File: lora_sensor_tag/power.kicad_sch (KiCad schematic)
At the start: 36 parts, among them J2 Li-ion_bat_conn, Q3 NPN, U5 TPS63070RNMR, U6 MCP73871-2CAI_ML, U7 AMS1117-3.3, U8 MAX17048G_T10

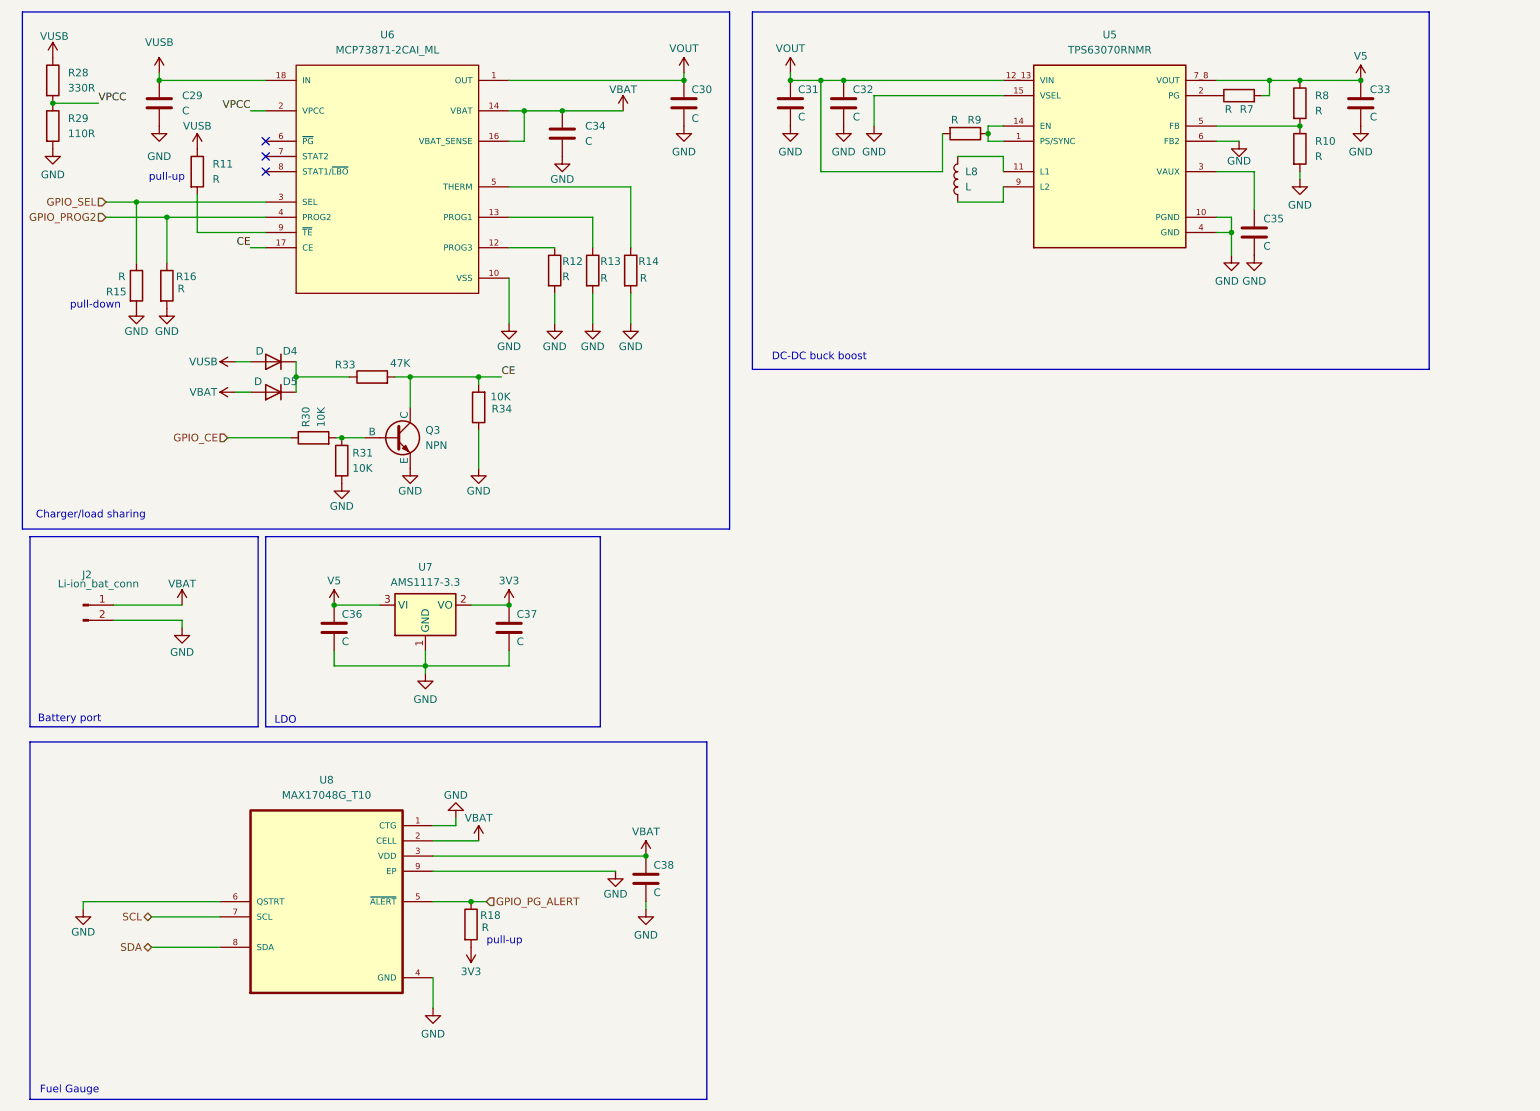
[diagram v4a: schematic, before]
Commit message: Large schematic update
This commit update the following:

 - Update MCP73871 CE control schematic
 - Finished schematic development and footprint
   assignment

Signed-off-by: Volodymyr <volodymyrnoha99@gmail.com>
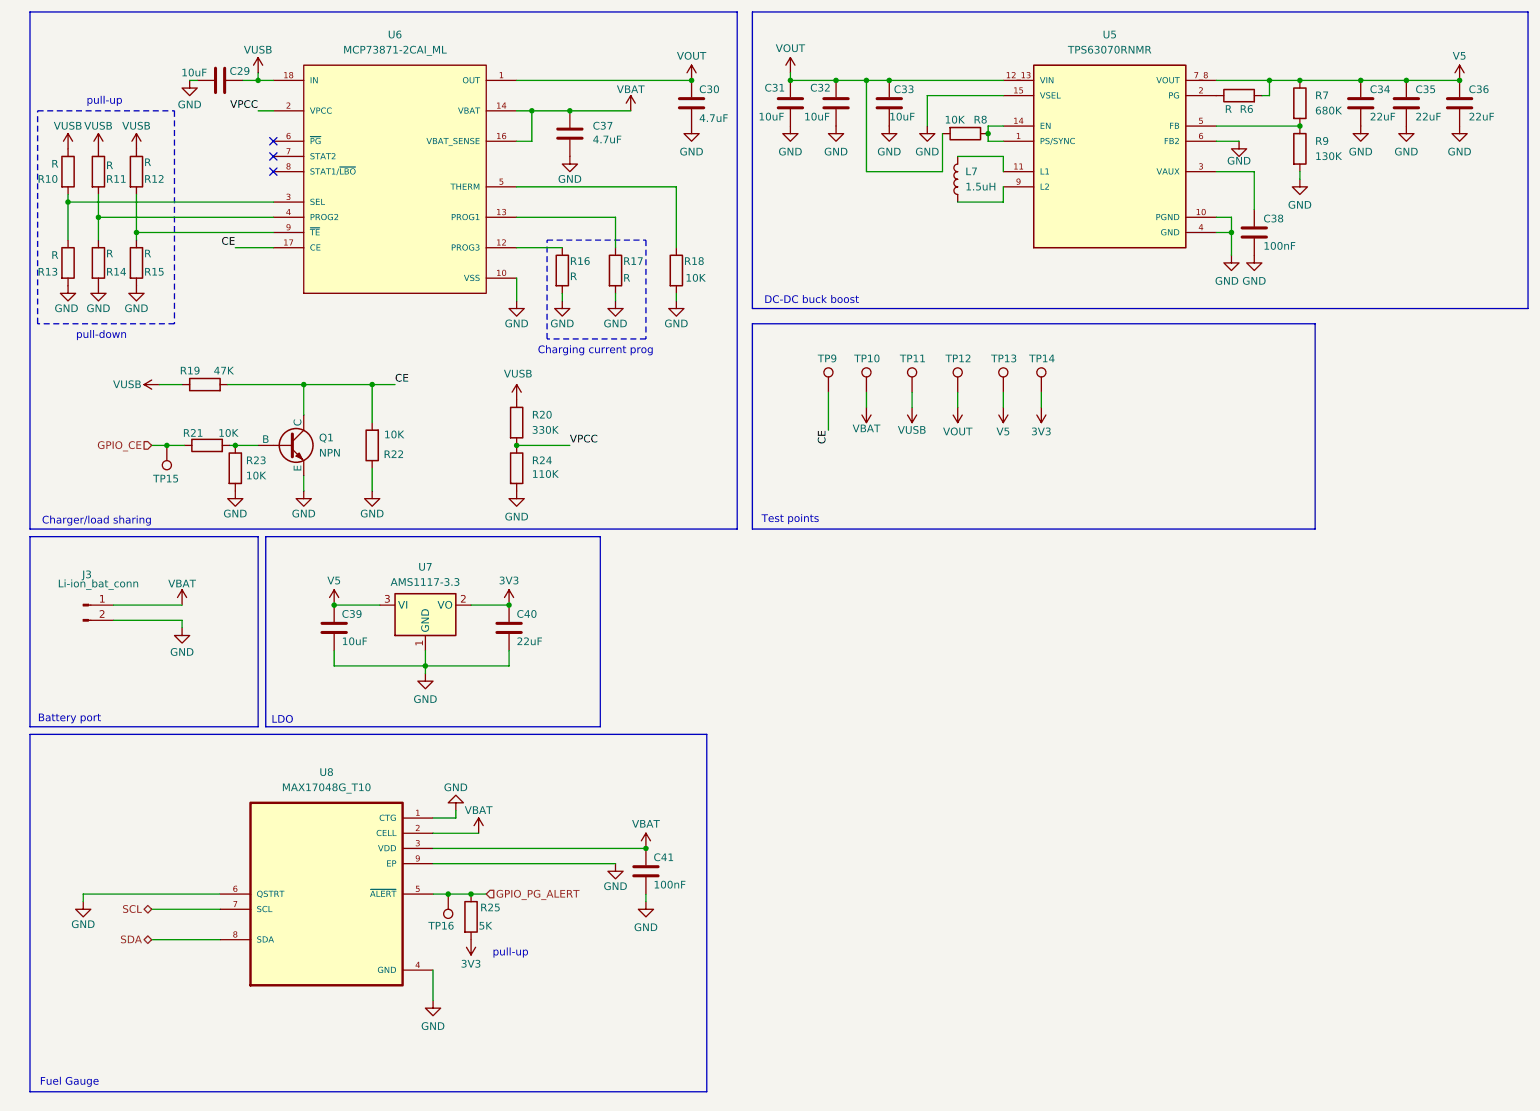
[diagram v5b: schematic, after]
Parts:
- removed D4, D5: D, symbol Device:D
- added C31: 10uF, Capacitor_SMD:C_0805_2012Metric, symbol Device:C
- added C35, C36: 22uF, Capacitor_SMD:C_0805_2012Metric, symbol Device:C
- added R10, R11, R15: R, Resistor_SMD:R_0603_1608Metric, symbol Device:R
- added TP10, TP11, TP12, TP13, TP14, TP15, TP16, TP9: TestPoint, TestPoint:TestPoint_Pad_D1.0mm, symbol Connector:TestPoint
- C29: value C -> 10uF; footprint (none) -> Capacitor_SMD:C_0603_1608Metric
- C30: value C -> 4.7uF; footprint MCP73871-2CAI_ML:QFN50P400X400X100-21N -> Capacitor_SMD:C_0603_1608Metric
- C32: renamed from C31; value C -> 10uF; footprint MCP73871-2CAI_ML:QFN50P400X400X100-21N -> Capacitor_SMD:C_0805_2012Metric
- C33: renamed from C32; value C -> 10uF; footprint MCP73871-2CAI_ML:QFN50P400X400X100-21N -> Capacitor_SMD:C_0603_1608Metric
- C34: renamed from C33; value C -> 22uF; footprint MCP73871-2CAI_ML:QFN50P400X400X100-21N -> Capacitor_SMD:C_0805_2012Metric
- C37: renamed from C34; value C -> 4.7uF; footprint (none) -> Capacitor_SMD:C_0603_1608Metric
- C38: renamed from C35; value C -> 100nF; footprint MCP73871-2CAI_ML:QFN50P400X400X100-21N -> Capacitor_SMD:C_0603_1608Metric
- C39: renamed from C36; value C -> 10uF; footprint MCP73871-2CAI_ML:QFN50P400X400X100-21N -> Capacitor_SMD:C_0603_1608Metric
- C40: renamed from C37; value C -> 22uF; footprint MCP73871-2CAI_ML:QFN50P400X400X100-21N -> Capacitor_SMD:C_0603_1608Metric
- C41: renamed from C38; value C -> 100nF; footprint MCP73871-2CAI_ML:QFN50P400X400X100-21N -> Capacitor_SMD:C_0603_1608Metric
- L7: renamed from L8; value L -> 1.5uH; footprint Relay_THT:Relay_DPDT_Finder_30.22 -> Inductor_SMD:L_Coilcraft_XxL4040
- Q1: renamed from Q3; footprint Package_DFN_QFN:Nordic_AQFN-94-1EP_7x7mm_P0.4mm -> Package_TO_SOT_SMD:SOT-23
- R12: renamed from R11; footprint TPS63070RNMR:VREG_TPS63070RNMR -> Resistor_SMD:R_0603_1608Metric
- R13: renamed from R15; footprint TPS63070RNMR:VREG_TPS63070RNMR -> Resistor_SMD:R_0603_1608Metric
- R14: renamed from R16; footprint TPS63070RNMR:VREG_TPS63070RNMR -> Resistor_SMD:R_0603_1608Metric
- R16: renamed from R12; footprint TPS63070RNMR:VREG_TPS63070RNMR -> Resistor_SMD:R_0603_1608Metric
- R17: renamed from R13; footprint TPS63070RNMR:VREG_TPS63070RNMR -> Resistor_SMD:R_0603_1608Metric
- R18: renamed from R14; value R -> 10K; footprint TPS63070RNMR:VREG_TPS63070RNMR -> Resistor_SMD:R_0603_1608Metric
- R19: renamed from R33; footprint TPS63070RNMR:VREG_TPS63070RNMR -> Resistor_SMD:R_0603_1608Metric
- R20: renamed from R28; value 330R -> 330K; footprint TPS63070RNMR:VREG_TPS63070RNMR -> Resistor_SMD:R_0603_1608Metric
- R21: renamed from R30; footprint TPS63070RNMR:VREG_TPS63070RNMR -> Resistor_SMD:R_0603_1608Metric
- R22: renamed from R34; footprint TPS63070RNMR:VREG_TPS63070RNMR -> Resistor_SMD:R_0603_1608Metric
- R23: renamed from R31; footprint TPS63070RNMR:VREG_TPS63070RNMR -> Resistor_SMD:R_0603_1608Metric
- R24: renamed from R29; value 110R -> 110K; footprint TPS63070RNMR:VREG_TPS63070RNMR -> Resistor_SMD:R_0603_1608Metric
- R25: renamed from R18; value R -> 5K; footprint TPS63070RNMR:VREG_TPS63070RNMR -> Resistor_SMD:R_0603_1608Metric
- R6: renamed from R7; footprint TPS63070RNMR:VREG_TPS63070RNMR -> Resistor_SMD:R_0603_1608Metric
- R7: renamed from R8; value R -> 680K; footprint TPS63070RNMR:VREG_TPS63070RNMR -> Resistor_SMD:R_0603_1608Metric
- R8: renamed from R9; value R -> 10K; footprint TPS63070RNMR:VREG_TPS63070RNMR -> Resistor_SMD:R_0603_1608Metric
- R9: renamed from R10; value R -> 130K; footprint TPS63070RNMR:VREG_TPS63070RNMR -> Resistor_SMD:R_0603_1608Metric
- renumbered J2 to J3
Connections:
- net 3V3: now also TP14.1
- net CE: now also TP9.1
- net GND: now also C29.1, C31.2, C35.2, C36.2, R15.2; no longer C29.2
- net GPIO_CE: now also TP15.1
- net GPIO_PG_ALERT: now also TP16.1
- net V5: now also C35.1, C36.1, TP13.1
- net VBAT: now also TP10.1
- net VOUT: now also C31.1, TP12.1
- net VUSB: now also C29.2, R19.1, R10.1, R11.1, TP11.1; no longer C29.1
- net at R12.2, U6.9 (~{TE}): now also R15.1
- net GPIO_PROG2: no longer names the net of R14.1, U6.4 (PROG2)
- net GPIO_PROG2: now also R11.2
- net GPIO_SEL: no longer names the net of R13.1, U6.3 (SEL)
- net GPIO_SEL: now also R10.2
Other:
- note added: "Charging current prog"
- note added: "Test points"
- moved on the sheet: C29, C30, C32, C33, C37, C41, Q1, R12, R13, R14, R16, R17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

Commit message: Update schematics
Adds the following updates to the schematics:
- Add power switch to the device;
- Add various LED indicators for device status monitoring;
- Add Reset and Prog buttons for device control;

Signed-off-by: Volodymyr <volodymyrnoha99@gmail.com>
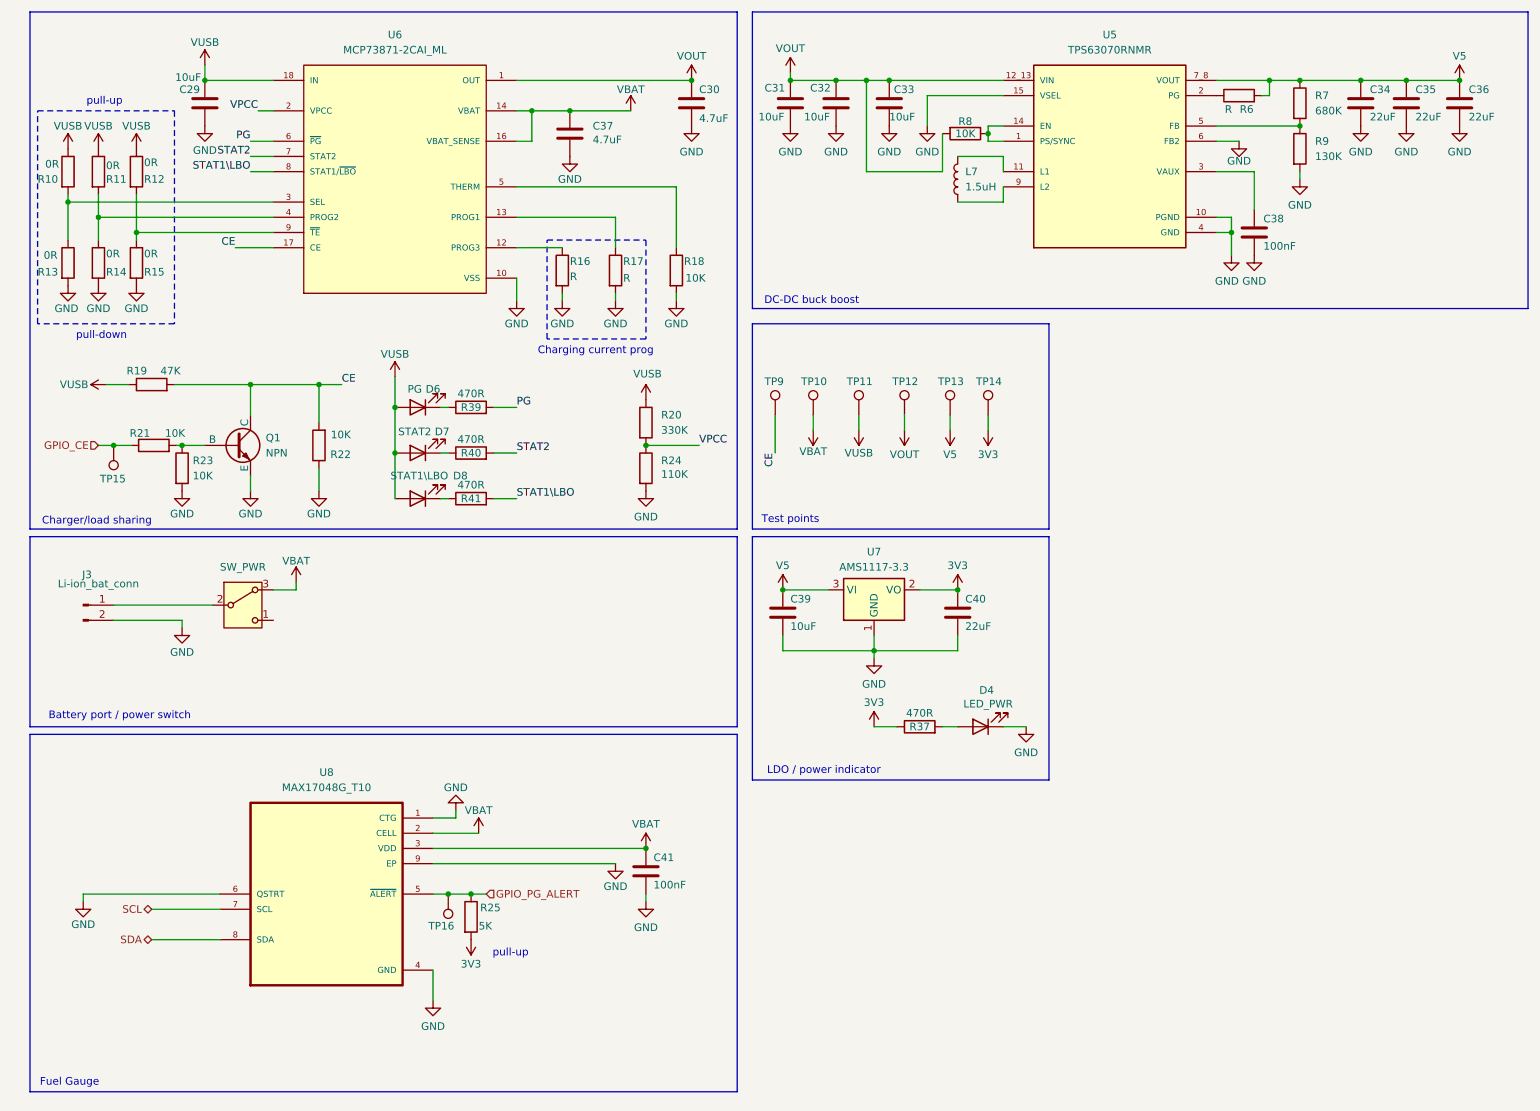
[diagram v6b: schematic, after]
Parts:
- added D4: LED_PWR, LED_SMD:LED_0603_1608Metrica, symbol Device:LED
- added D6: PG, LED_SMD:LED_0603_1608Metrica, symbol Device:LED
- added D7: STAT2, LED_SMD:LED_0603_1608Metrica, symbol Device:LED
- added D8: STAT1\LBO, LED_SMD:LED_0603_1608Metrica, symbol Device:LED
- added R37, R39, R40, R41: 470R, Resistor_SMD:R_0603_1608Metric, symbol Device:R
- added SW_PWR: SW_Nidec_CAS-120A1, Button_Switch_SMD:Nidec_Copal_CAS-120A, symbol Switch:SW_Nidec_CAS-120A1
- R10, R11, R12, R13, R14, R15: value R -> 0R
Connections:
- net 3V3: now also R37.1
- net GND: now also D4.1 (K)
- net VBAT: now also SW_PWR.3 (A); no longer J3.1 (Pin_1)
- net VUSB: now also D6.2 (A), D7.2 (A), D8.2 (A)
- net PG: now reaches U6.6 (~{PG})
- net PG: now also R39.2
- net STAT2: now reaches U6.7 (STAT2)
- net STAT2: now also R40.2
- net STAT1\LBO: now reaches U6.8 (STAT1/~{LBO})
- net STAT1\LBO: now also R41.2
- new net: J3.1 (Pin_1), SW_PWR.2 (B)
- new net: D7.1 (K), R40.1
- new net: D4.2 (A), R37.2
- new net: D6.1 (K), R39.1
- new net: D8.1 (K), R41.1
- no-connect marks 3 -> 0
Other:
- note added: "Battery port / power switch"
- note added: "LDO / power indicator"
- note removed: "Battery port"
- note removed: "LDO"
- moved on the sheet: C29, C39, C40, Q1, R19, R20, R21, R22, R23, R24, TP10, TP11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

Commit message: pcb_layout: Add initial board layout
Adds:
 - Initial board dimensions;
 - Initial MCU component placement and routing

Signed-off-by: Volodymyr <volodymyrnoha99@gmail.com>
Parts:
- renumbered C29 to C31, C30 to C32, C31 to C33, C32 to C34, C33 to C35, C34 to C36, C35 to C37, C36 to C38, C37 to C39, C38 to C40, C39 to C41, C40 to C42, C41 to C43, D6 to D2, D7 to D3, D8 to D4, D4 to D5, R7 to R10, R8 to R11, R9 to R12, R10 to R13, R11 to R14, R12 to R15, R13 to R16, R14 to R17, R15 to R18, R16 to R19, R17 to R20, R18 to R21, R19 to R22, R39 to R23, R20 to R24, R21 to R25, R22 to R26, R40 to R27, R23 to R28, R24 to R29, R41 to R30, R37 to R31, R25 to R32, R6 to R9, SW_PWR to SW_PWR1
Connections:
- no-connect marks 0 -> 1
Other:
- moved on the sheet: D5, R31

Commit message: Update PCB layout routing
Updates and adds the following changes to the PCB
layout routing:
- Changed board dimensions and topology;
- Add layout for MCP73871 Li-ion battery charger;
- Add layout for MAX17048 Fuel Gauge;

Signed-off-by: Volodymyr <volodymyrnoha99@gmail.com>
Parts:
- D2, D3, D4, D5: footprint LED_SMD:LED_0603_1608Metrica -> LED_SMD:LED_0603_1608Metric
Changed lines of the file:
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@@
 			)
 		)
-		(property "Footprint" "LED_SMD:LED_0603_1608Metrica"
+		(property "Footprint" "LED_SMD:LED_0603_1608Metric"
 			(at 166.37 133.35 0)
 			(hide yes)
@@
 			)
 		)
-		(property "Footprint" "LED_SMD:LED_0603_1608Metrica"
+		(property "Footprint" "LED_SMD:LED_0603_1608Metric"
 			(at 80.01 95.25 0)
 			(hide yes)
@@
 			)
 		)
-		(property "Footprint" "LED_SMD:LED_0603_1608Metrica"
+		(property "Footprint" "LED_SMD:LED_0603_1608Metric"
 			(at 80.01 87.63 0)
 			(hide yes)
@@
 			)
 		)
-		(property "Footprint" "LED_SMD:LED_0603_1608Metrica"
+		(property "Footprint" "LED_SMD:LED_0603_1608Metric"
 			(at 80.01 80.01 0)
 			(hide yes)
